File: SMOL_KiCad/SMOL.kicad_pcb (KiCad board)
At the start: 2 copper layers, 14.2 x 13.2 mm, 17 parts, among them J1 Conn_01x05, U1 TLV61220, U2 ATTINY10-TS

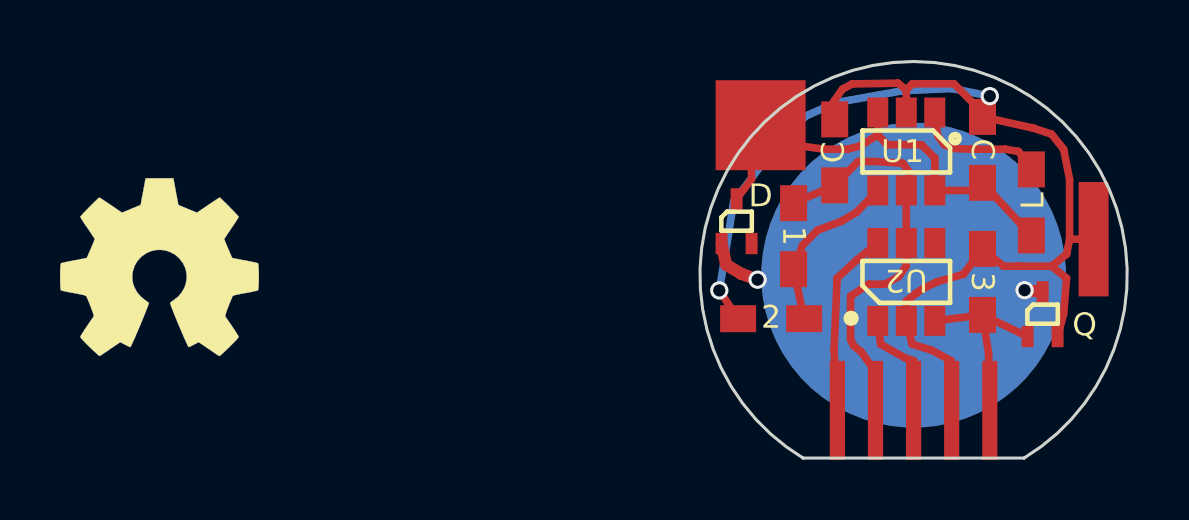
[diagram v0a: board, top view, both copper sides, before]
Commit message: Update spinning render
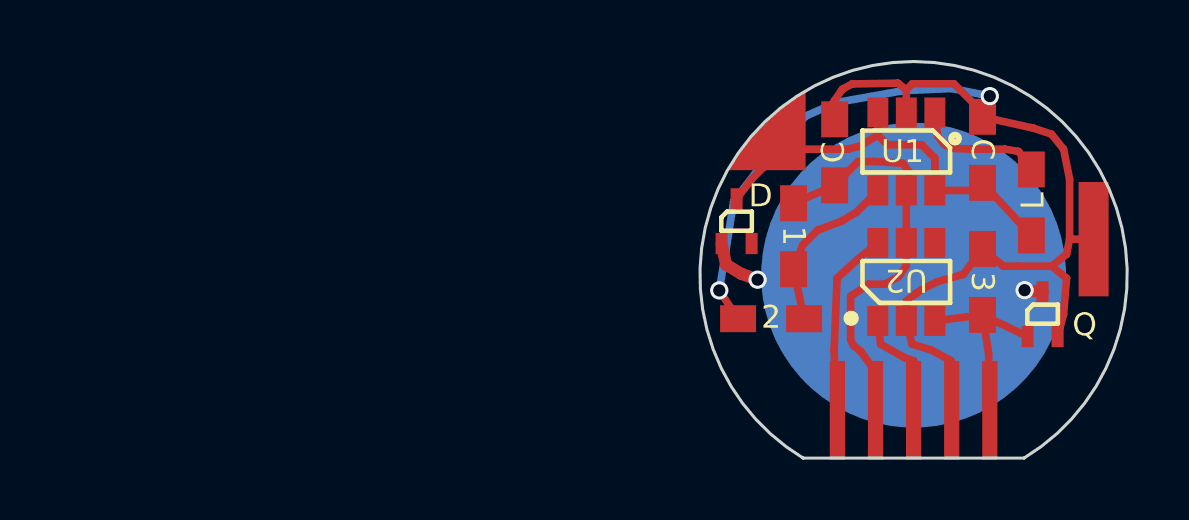
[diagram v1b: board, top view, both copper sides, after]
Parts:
- removed REF***: OSHW-Symbol_6.7x6mm_SilkScreen, Symbols:OSHW-Symbol_6.7x6mm_SilkScreen

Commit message: re-jigging the form factor of circuit revision 6
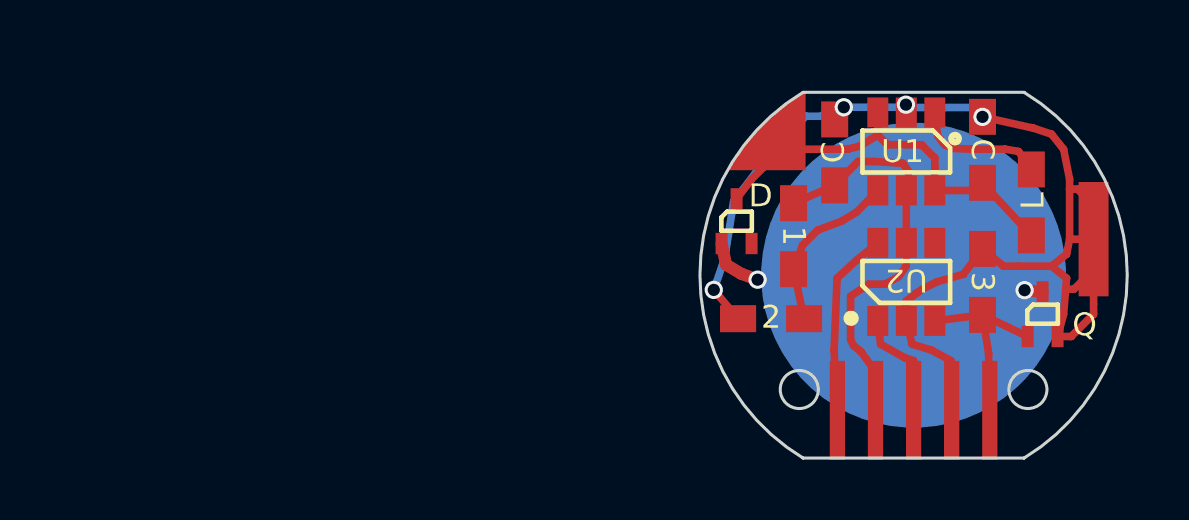
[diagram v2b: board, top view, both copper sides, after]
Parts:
- moved G*** 0.13 mm to (101.6, 101.6), turned to 258 degrees
- turned G*** to 100 degrees
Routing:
- net /Anode: track 43.5 -> 45.8 mm, vias 2 -> 4
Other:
- board size 14.2 x 13.2 mm -> 14.2 x 12.2 mm

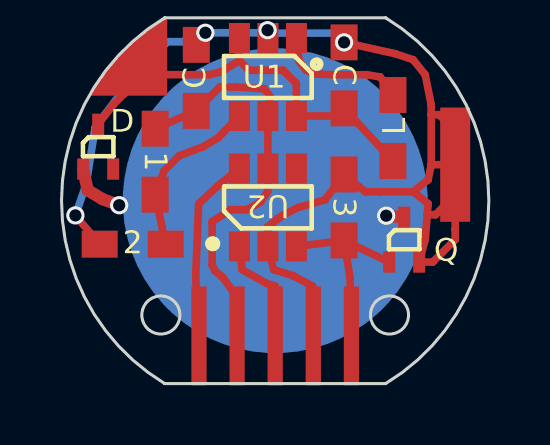
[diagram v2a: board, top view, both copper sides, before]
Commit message: re-sized mounting holes to fit M1.4 bolts, like in japanese watches. Everyone has m1.4 bolts handy, right?
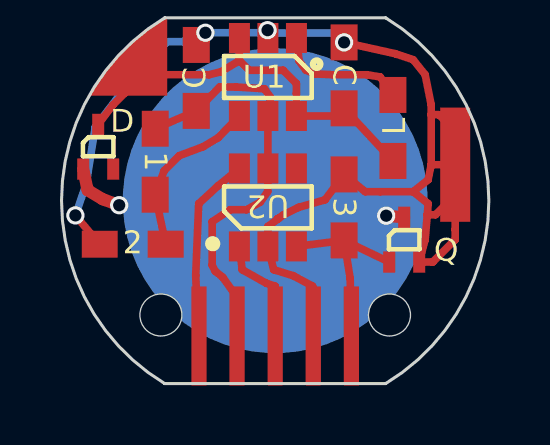
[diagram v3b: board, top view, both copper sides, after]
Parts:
- added REF**: SolderWirePad_single_2mmDrill, Wire_Pads:SolderWirePad_single_2mmDrill, F.Cu at (105.0, 112.1)
- added REF**: SolderWirePad_single_2mmDrill, Wire_Pads:SolderWirePad_single_2mmDrill, F.Cu at (94.2, 110.4)
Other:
- outline, holes or cut-outs redrawn
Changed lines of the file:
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@@
   (general
     (thickness 0.508)
-    (drawings 8)
+    (drawings 6)
     (tracks 133)
     (zones 0)
-    (modules 16)
+    (modules 18)
     (nets 10)
   )
@@
   (layers
     (0 F.Cu signal)
-    (31 B.Cu signal hide)
+    (31 B.Cu signal)
     (36 B.SilkS user)
     (37 F.SilkS user)
@@
     (mod_text_size 1 1)
     (mod_text_width 0.15)
-    (pad_size 0.1 0.1)
-    (pad_drill 0)
+    (pad_size 1.4 1.4)
+    (pad_drill 1.4)
     (pad_to_mask_clearance 0.0508)
     (solder_mask_min_width 0.25)
     (aux_axis_origin 0 0)
-    (visible_elements 7FEFF77F)
+    (visible_elements 7FFFF77F)
     (pcbplotparams
       (layerselection 0x010f0_ffffffff)
@@
     (uvia_dia 0.3048)
     (uvia_drill 0.1016)
+  )
+  (module Wire_Pads:SolderWirePad_single_2mmDrill (layer F.Cu)
+    (at 105.029 112.141)
+    (fp_text reference REF** (at 0 -3.81) (layer F.SilkS) hide
+      (effects (font (size 1 1) (thickness 0.15)))
+    )
+    (fp_text value SolderWirePad_single_2mmDrill (at -0.635 3.81) (layer F.Fab)
+      (effects (font (size 1 1) (thickness 0.15)))
+    )
+    (pad "" np_thru_hole circle (at 0.381 -6.731) (size 1.4 1.4) (drill 1.4) (layers *.Cu *.Mask))
   )
   (module SMOL_footprints:credits2-title (layer B.Cu)
@@
       (xy -4.639425 3.518309) (xy -4.711621 3.553449) (xy -4.791467 3.60512) (xy -4.882889 3.675701)) (layer B.SilkS) (width 0.01))
   )
-  (gr_circle (center 97.79 105.41) (end 98.425 105.41) (layer Edge.Cuts) (width 0.1016))
-  (gr_circle (center 105.41 105.41) (end 106.045 105.41) (layer Edge.Cuts) (width 0.1016))
+  (module Wire_Pads:SolderWirePad_single_2mmDrill (layer F.Cu)
+    (at 94.234 110.363)
+    (fp_text reference REF** (at 0 -3.81) (layer F.SilkS) hide
+      (effects (font (size 1 1) (thickness 0.15)))
+    )
+    (fp_text value SolderWirePad_single_2mmDrill (at -0.635 3.81) (layer F.Fab)
+      (effects (font (size 1 1) (thickness 0.15)))
+    )
+    (pad "" np_thru_hole circle (at 3.556 -4.953) (size 1.4 1.4) (drill 1.4) (layers *.Cu *.Mask))
+  )
   (gr_arc (start 101.6 101.6) (end 105.283 107.696) (angle -117.7) (layer Edge.Cuts) (width 0.1016))
   (gr_line (start 97.917 95.504) (end 105.283 95.504) (angle 90) (layer Edge.Cuts) (width 0.1016))

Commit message: Revision 6c - use pogo pins for programming AND alignment
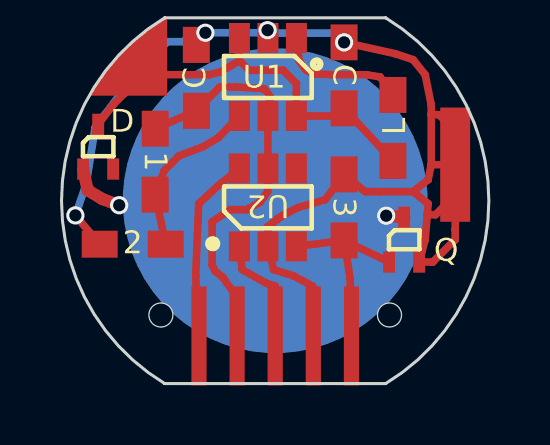
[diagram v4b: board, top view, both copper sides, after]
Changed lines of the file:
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@@
     (mod_text_size 1 1)
     (mod_text_width 0.15)
-    (pad_size 1.4 1.4)
-    (pad_drill 1.4)
+    (pad_size 0.8 0.8)
+    (pad_drill 0.8)
     (pad_to_mask_clearance 0.0508)
     (solder_mask_min_width 0.25)
@@
       (effects (font (size 1 1) (thickness 0.15)))
     )
-    (pad "" np_thru_hole circle (at 0.381 -6.731) (size 1.4 1.4) (drill 1.4) (layers *.Cu *.Mask))
+    (pad "" np_thru_hole circle (at 0.381 -6.731) (size 0.8 0.8) (drill 0.8) (layers *.Cu *.Mask))
   )
   (module SMOL_footprints:credits2-title (layer B.Cu)
@@
       (effects (font (size 1 1) (thickness 0.15)))
     )
-    (pad "" np_thru_hole circle (at 3.556 -4.953) (size 1.4 1.4) (drill 1.4) (layers *.Cu *.Mask))
+    (pad "" np_thru_hole circle (at 3.556 -4.953) (size 0.8 0.8) (drill 0.8) (layers *.Cu *.Mask))
   )
   (gr_arc (start 101.6 101.6) (end 105.283 107.696) (angle -117.7) (layer Edge.Cuts) (width 0.1016))

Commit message: FINALLY fixed the anchor points for mounting holes on SMOL and programmers. Added OSHW logo to library, just in case....
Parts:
- removed REF**: SolderWirePad_single_2mmDrill, Wire_Pads:SolderWirePad_single_2mmDrill
- added HOLE2: SolderWirePad_single_2mmDrill, Wire_Pads:SolderWirePad_single_2mmDrill, F.Cu at (105.4, 105.4)
- moved HOLE1 6.10 mm to (97.8, 105.4)
- renumbered G*** to GFX1, G*** to GFX2, REF** to HOLE1
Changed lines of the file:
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@@
-(kicad_pcb (version 20171130) (host pcbnew "(5.0.2)-1")
+(kicad_pcb (version 20171130) (host pcbnew "(5.1.2)-1")
   (general
     (thickness 0.508)
@@
   (layers
     (0 F.Cu signal)
-    (31 B.Cu signal)
+    (31 B.Cu signal hide)
     (36 B.SilkS user)
     (37 F.SilkS user)
@@
     (zone_45_only no)
     (trace_min 0.2)
-    (segment_width 0.1016)
-    (edge_width 0.1016)
     (via_size 0.6096)
     (via_drill 0.4064)
@@
     (uvia_min_size 0.2)
     (uvia_min_drill 0.1)
+    (edge_width 0.1016)
+    (segment_width 0.1016)
     (pcb_text_width 0.3)
     (pcb_text_size 1.5 1.5)
@@
     (solder_mask_min_width 0.25)
     (aux_axis_origin 0 0)
-    (visible_elements 7FFFF77F)
+    (visible_elements 7FFFFF7F)
     (pcbplotparams
       (layerselection 0x010f0_ffffffff)
@@
   )
   (module Wire_Pads:SolderWirePad_single_2mmDrill (layer F.Cu)
-    (at 105.029 112.141)
-    (fp_text reference REF** (at 0 -3.81) (layer F.SilkS) hide
+    (at 105.41 105.41)
+    (fp_text reference HOLE2 (at 0 -3.81) (layer F.SilkS) hide
       (effects (font (size 1 1) (thickness 0.15)))
     )
@@
       (effects (font (size 1 1) (thickness 0.15)))
     )
-    (pad "" np_thru_hole circle (at 0.381 -6.731) (size 0.8 0.8) (drill 0.8) (layers *.Cu *.Mask))
+    (pad "" np_thru_hole circle (at 0 0) (size 0.8 0.8) (drill 0.8) (layers *.Cu *.Mask))
   )
   (module SMOL_footprints:credits2-title (layer B.Cu)
     (at 101.6 101.727 100)
-    (fp_text reference G*** (at -14.859 10.795 100) (layer B.SilkS) hide
+    (fp_text reference GFX2 (at -14.859 10.795 100) (layer B.SilkS) hide
       (effects (font (size 1.524 1.524) (thickness 0.3)) (justify mirror))
     )
@@
   (module SMOL_footprints:credits2-name (layer B.Cu)
     (at 101.6 101.6 258)
-    (fp_text reference G*** (at -14.859 10.795 258) (layer B.SilkS) hide
+    (fp_text reference GFX1 (at -14.859 10.795 258) (layer B.SilkS) hide
       (effects (font (size 1.524 1.524) (thickness 0.3)) (justify mirror))
     )
@@
   )
   (module Wire_Pads:SolderWirePad_single_2mmDrill (layer F.Cu)
-    (at 94.234 110.363)
-    (fp_text reference REF** (at 0 -3.81) (layer F.SilkS) hide
+    (at 97.79 105.41)
+    (fp_text reference HOLE1 (at 0 -3.81) (layer F.SilkS) hide
       (effects (font (size 1 1) (thickness 0.15)))
     )
@@
       (effects (font (size 1 1) (thickness 0.15)))
     )
-    (pad "" np_thru_hole circle (at 3.556 -4.953) (size 0.8 0.8) (drill 0.8) (layers *.Cu *.Mask))
+    (pad "" np_thru_hole circle (at 0 0) (size 0.8 0.8) (drill 0.8) (layers *.Cu *.Mask))
   )
   (gr_arc (start 101.6 101.6) (end 105.283 107.696) (angle -117.7) (layer Edge.Cuts) (width 0.1016))

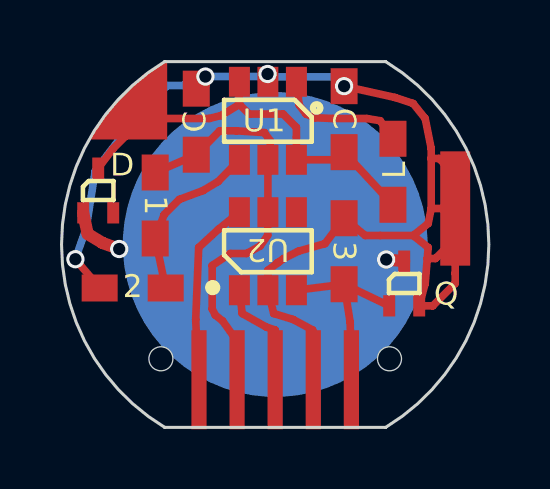
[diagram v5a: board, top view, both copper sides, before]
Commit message: Revision seven! Added a small resistor to protect the MOSFET.
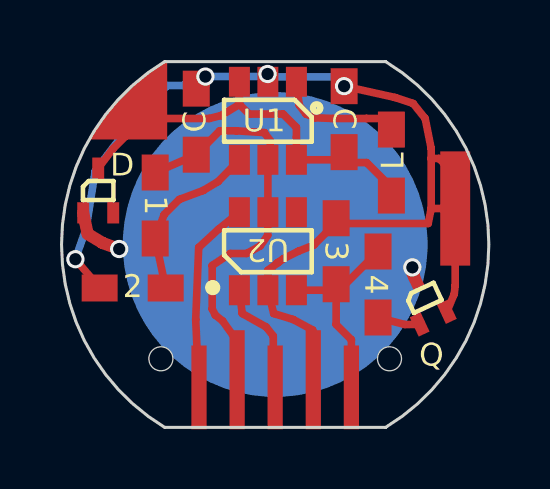
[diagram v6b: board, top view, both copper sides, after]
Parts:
- added 4: 1kΩ, SMOL_footprints:0603_HandSoldering, F.Cu at (105.0, 102.9)
- moved Q 0.81 mm to (106.6, 103.4), turned to 25 degrees
- moved L 0.31 mm to (105.5, 98.9)
- moved 3 0.27 mm to (103.6, 101.8)
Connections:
- 3 pad 2: Net-(Q1-Pad1) -> Net-(J1-Pad5)
- J1 pad 5: Net-(Q1-Pad1) -> Net-(J1-Pad5)
- U2 pad 3: Net-(Q1-Pad1) -> Net-(J1-Pad5)
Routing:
- net Net-(J1-Pad5): track 0.00 -> 6.89 mm
- net /Anode: track 45.8 -> 40.2 mm
- net Net-(Q1-Pad1): track 6.85 -> 1.42 mm
- net Net-(J1-Pad3): track 5.56 -> 3.74 mm
- net /Spring_Contact: track 11.4 -> 12.1 mm
